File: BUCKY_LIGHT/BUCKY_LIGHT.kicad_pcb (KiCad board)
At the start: 2 copper layers, 145 x 130 mm, 150 parts, among them J1 CAN_CONN, J2 SERIAL_CONN, Q1 Q_Photo_NPN, Q10 Q_Photo_NPN, Q11 Q_Photo_NPN, Q12 Q_Photo_NPN, Q13 Q_Photo_NPN, Q14 Q_Photo_NPN, Q15 Q_Photo_NPN, Q16 Q_Photo_NPN, Q17 Q_Photo_NPN, Q18 Q_Photo_NPN, Q19 Q_Photo_NPN, Q2 Q_Photo_NPN, Q20 Q_Photo_NPN, Q21 Q_Photo_NPN, Q22 Q_Photo_NPN, Q23 Q_Photo_NPN, Q24 Q_Photo_NPN, Q25 Q_Photo_NPN, Q26 Q_Photo_NPN, Q27 Q_Photo_NPN, Q28 Q_Photo_NPN, Q3 Q_Photo_NPN, Q4 Q_Photo_NPN, Q5 Q_Photo_NPN, Q6 Q_Photo_NPN, Q7 Q_Photo_NPN, Q8 Q_Photo_NPN, Q9 Q_Photo_NPN, U1 FRONT, U2 RIGHT, U3 DOWN, U4 LEFT, U5 SN65HVD230, U6 ESP32-WROOM-32U

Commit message: Some IR changes
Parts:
- removed C1, C10, C11, C12, C13, C14, C15, C16, C17, C18, C19, C2, C20, C21, C22, C23, C24, C25, C26, C27, C28, C3, C4, C5, C6, C7, C8, C9: 0.1u, Capacitor_SMD:C_0805_2012Metric_Pad1.18x1.45mm_HandSolder
- removed R65: 120R, Resistor_SMD:R_0805_2012Metric_Pad1.20x1.40mm_HandSolder
- removed R66: 10k, Resistor_SMD:R_0805_2012Metric_Pad1.20x1.40mm_HandSolder
- moved J1 103.7 mm to (158.1, 106.5)

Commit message: Some LIGHT dev
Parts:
- added C1: 22u, Capacitor_SMD:C_1210_3225Metric_Pad1.33x2.70mm_HandSolder, F.Cu at (169.7, 104.8)
- added C2: 0.1u, Capacitor_SMD:C_1210_3225Metric_Pad1.33x2.70mm_HandSolder, F.Cu at (159.8, 113.1)
- added C3: 10u, Capacitor_SMD:C_1210_3225Metric_Pad1.33x2.70mm_HandSolder, F.Cu at (175.7, 104.8)
- added C4: 0.1u, Capacitor_SMD:C_1210_3225Metric_Pad1.33x2.70mm_HandSolder, F.Cu at (165.8, 113.1)
- added R65: 120R, Resistor_SMD:R_0805_2012Metric_Pad1.20x1.40mm_HandSolder, F.Cu at (169.0, 108.5)
- added R66: 10k, Resistor_SMD:R_0805_2012Metric_Pad1.20x1.40mm_HandSolder, F.Cu at (171.2, 111.4)
- added U7: AMS1117-3.3, Package_TO_SOT_SMD:SOT-223-3_TabPin2, F.Cu at (161.7, 106.8)
- U5, U6: moved to B.Cu
- moved J2 43.1 mm to (111.5, 118.2), turned to -90 degrees
- moved J1 14.8 mm to (143.4, 108.0)
- moved U6 14.1 mm to (143.3, 90.6), turned to 180 degrees
- moved U5 12.9 mm to (143.2, 119.8), turned to 180 degrees
- moved R54 0.81 mm to (178.5, 161.0)
- moved R38 0.76 mm to (185.5, 48.0)
- moved R8 0.76 mm to (101.0, 159.5)
- moved R14 0.72 mm to (76.5, 129.0)
- moved R5 0.70 mm to (139.8, 161.0)
- moved R55 0.70 mm to (166.2, 161.0)
- moved R56 0.70 mm to (153.3, 161.0)
- moved R6 0.70 mm to (126.3, 161.0)
- moved R7 0.70 mm to (113.3, 161.0)
- moved R15 0.67 mm to (73.0, 115.5)
- moved R37 0.64 mm to (173.5, 41.0)
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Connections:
- R13 pad 1: +3V3 -> +5V
- R14 pad 1: +3V3 -> +5V
- R15 pad 1: +3V3 -> +5V
- R16 pad 1: +3V3 -> +5V
- R21 pad 1: +3V3 -> +5V
- R22 pad 1: +3V3 -> +5V
- R23 pad 1: +3V3 -> +5V
- R24 pad 1: +3V3 -> +5V
- R29 pad 1: +3V3 -> +5V
- R30 pad 1: +3V3 -> +5V
- R31 pad 1: +3V3 -> +5V
- R32 pad 1: +3V3 -> +5V
- R37 pad 1: +3V3 -> +5V
- R38 pad 1: +3V3 -> +5V
- R39 pad 1: +3V3 -> +5V
- R40 pad 1: +3V3 -> +5V
- R45 pad 1: +3V3 -> +5V
- R46 pad 1: +3V3 -> +5V
- R47 pad 1: +3V3 -> +5V
- R48 pad 1: +3V3 -> +5V
- R5 pad 1: +3V3 -> +5V
- R53 pad 1: +3V3 -> +5V
- R54 pad 1: +3V3 -> +5V
- R55 pad 1: +3V3 -> +5V
- R56 pad 1: +3V3 -> +5V
- R6 pad 1: +3V3 -> +5V
- R7 pad 1: +3V3 -> +5V
- R8 pad 1: +3V3 -> +5V
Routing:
- net +5V: track 0.00 -> 881.1 mm, vias 0 -> 32
- net +3V3: track 0.00 -> 400.3 mm, vias 0 -> 28
- net Net-(D4-Pad2): track 0.00 -> 3.62 mm
- net Net-(D16-Pad2): track 0.00 -> 3.20 mm
- net Net-(D26-Pad2): track 0.00 -> 3.07 mm
- net Net-(D20-Pad2): track 0.00 -> 3.00 mm
- net Net-(D21-Pad2): track 0.00 -> 2.95 mm
- net Net-(D14-Pad2): track 0.00 -> 2.94 mm
- net Net-(D7-Pad2): track 0.00 -> 2.86 mm
- net Net-(D22-Pad2): track 0.00 -> 2.76 mm
- net Net-(D3-Pad2): track 0.00 -> 2.74 mm
- net Net-(D2-Pad2): track 0.00 -> 2.70 mm
- net Net-(D1-Pad2): track 0.00 -> 2.68 mm
- net Net-(D27-Pad2): track 0.00 -> 2.67 mm
- net Net-(D28-Pad2): track 0.00 -> 2.66 mm
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
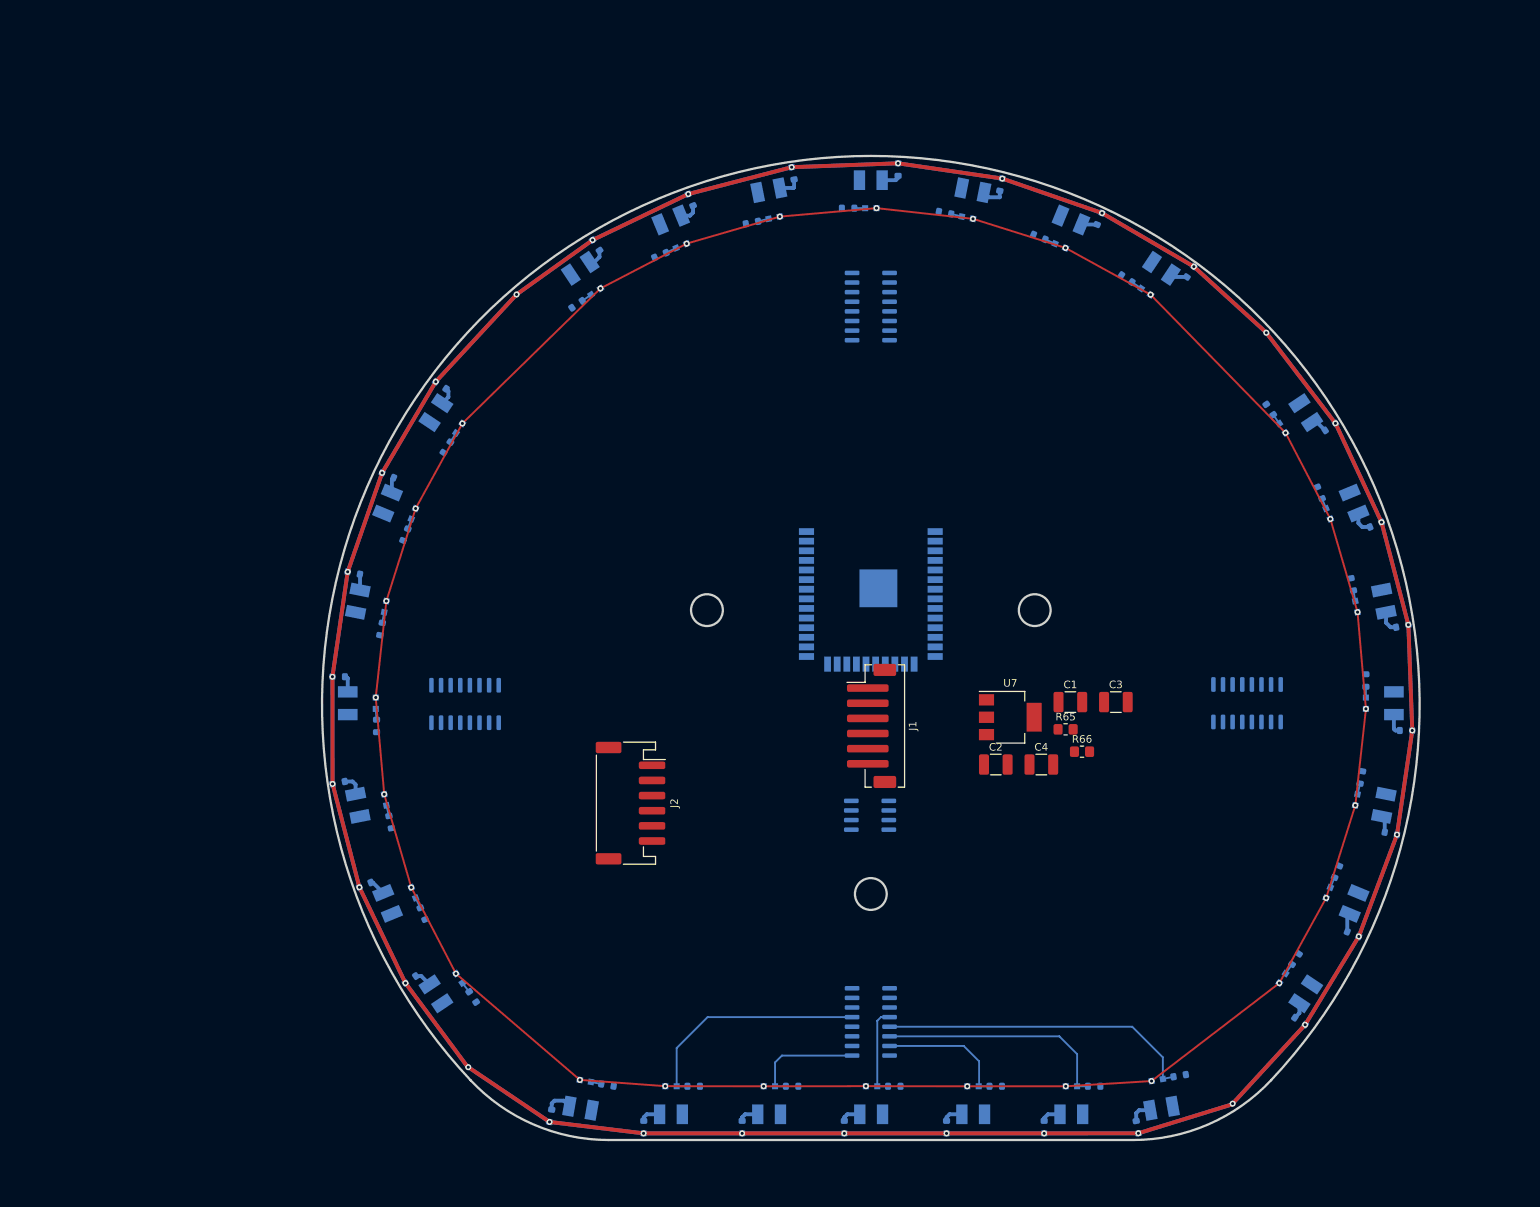
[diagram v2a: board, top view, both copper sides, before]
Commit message: Finished bulk of LIGHT, only REF left
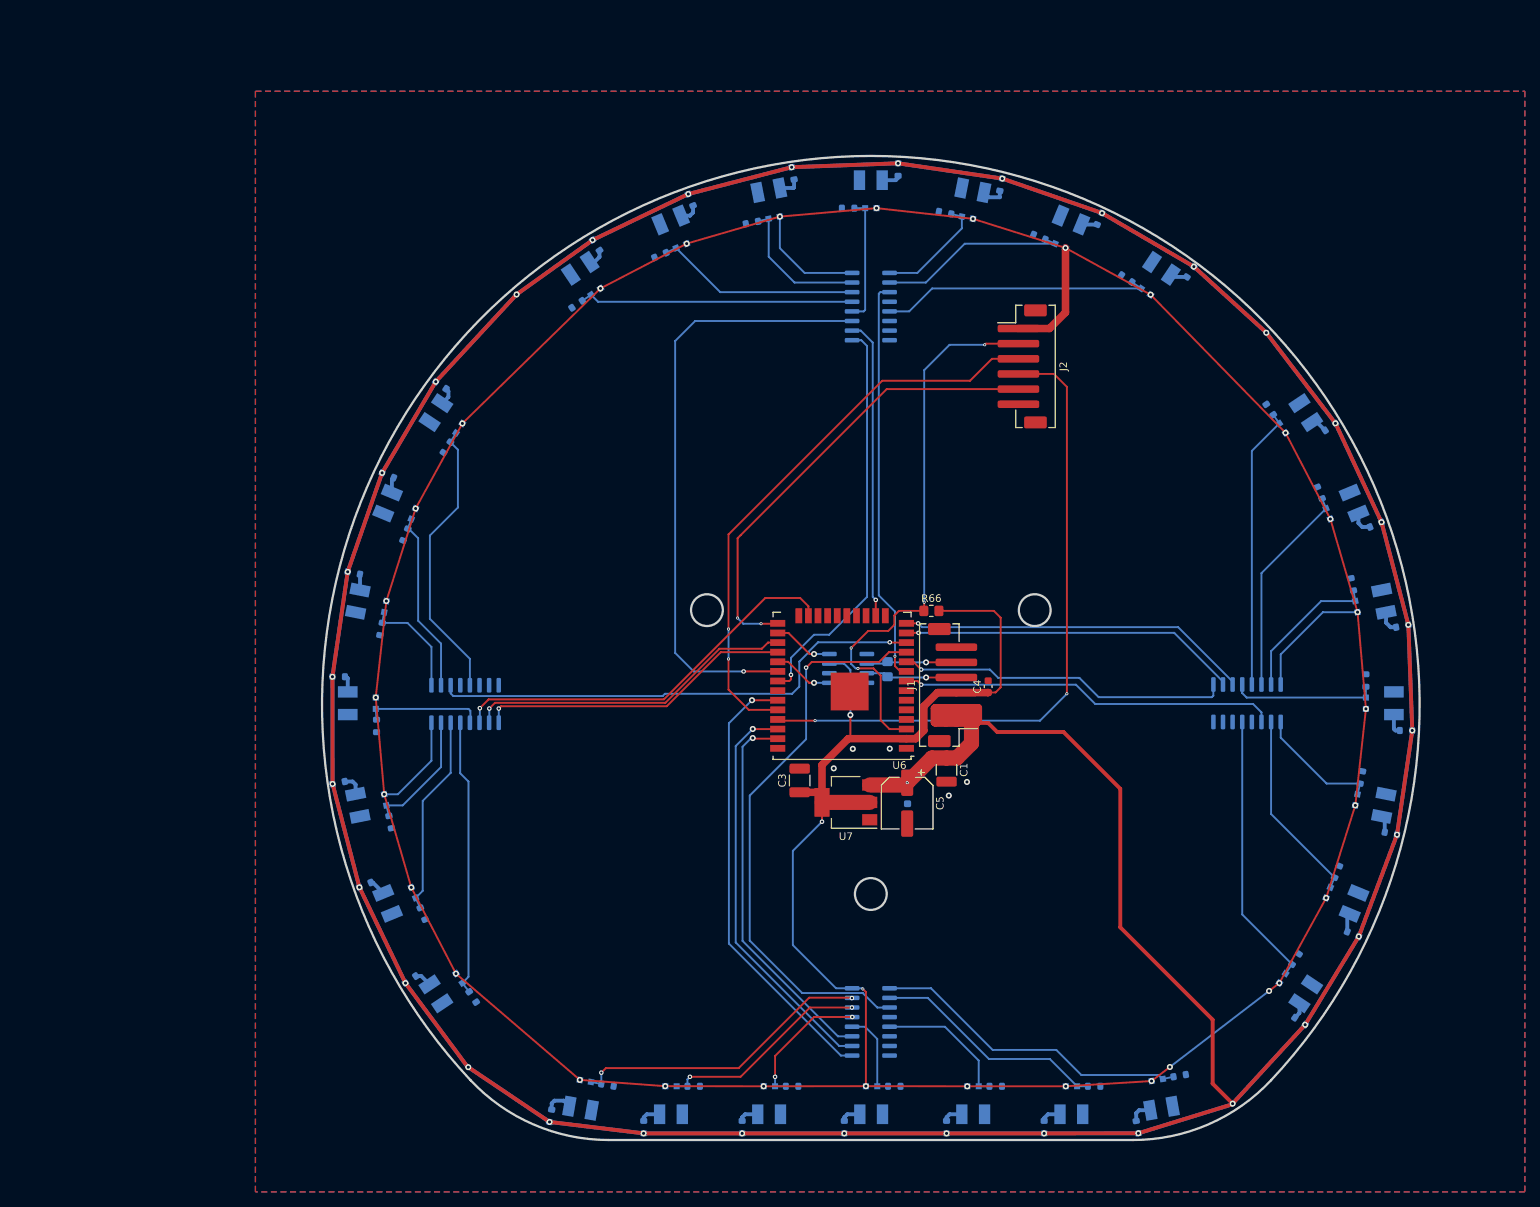
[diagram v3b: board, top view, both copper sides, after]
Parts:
- added C5: 100u, Capacitor_SMD:CP_Elec_6.3x7.7, F.Cu at (148.1, 118.2)
- C2: footprint Capacitor_SMD:C_1210_3225Metric_Pad1.33x2.70mm_HandSolder -> Capacitor_SMD:C_0603_1608Metric; moved to B.Cu
- C4: footprint Capacitor_SMD:C_1210_3225Metric_Pad1.33x2.70mm_HandSolder -> Capacitor_SMD:C_0603_1608Metric
- J2: footprint Connector_JST:JST_PH_S6B-PH-SM4-TB_1x06-1MP_P2.00mm_Horizontal -> Connector_JST:JST_PH_B6B-PH-SM4-TB_1x06-1MP_P2.00mm_Vertical
- R65: moved to B.Cu
- U6: moved to F.Cu
- moved J2 77.5 mm to (163.3, 60.5)
- moved C3 43.0 mm to (133.9, 115.2), turned to 90 degrees
- moved R66 27.2 mm to (151.3, 92.8)
- moved R65 24.8 mm to (145.5, 100.5), turned to 90 degrees
- moved U7 24.5 mm to (140.0, 118.1), turned to 180 degrees
- moved U5 19.6 mm to (140.3, 100.4), turned to 0 degrees
- moved C1 18.6 mm to (153.3, 113.8), turned to -90 degrees
- moved U6 12.7 mm to (139.5, 102.7)
- moved C4 12.5 mm to (158.8, 102.8), turned to 90 degrees
- moved C2 12.5 mm to (148.2, 117.5), turned to -90 degrees
- moved J1 12.0 mm to (154.1, 102.6), turned to 90 degrees
- turned U1 to 180 degrees
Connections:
- U1 pad 1: L2 -> L26
- U1 pad 13: L26 -> L2
- U1 pad 14: L27 -> L3
- U1 pad 15: L28 -> L4
- U1 pad 2: L4 -> L27
- U1 pad 5: L3 -> L28
- U2 pad 2: L11 -> L10
- U2 pad 5: L10 -> L11
- U3 pad 2: L18 -> L17
- U3 pad 5: L17 -> L18
- U4 pad 2: L25 -> L24
- U4 pad 5: L24 -> L25
- U6 pad 10: D_S2 -> L_S2
- U6 pad 13: F_S2 -> L_S1
- U6 pad 14: F_S0 -> L_S0
- U6 pad 16: F_S1 -> D_S1
- U6 pad 26: unconnected-(U6-Pad26) -> /CAN_RX
- U6 pad 29: unconnected-(U6-Pad29) -> /CAN_TX
- U6 pad 30: L_S0 -> D_S0
- U6 pad 31: L_S1 -> D_S2
- U6 pad 33: L_S2 -> F_S2
- U6 pad 36: D_S0 -> F_S1
- U6 pad 37: D_S1 -> F_S0
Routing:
- net +3V3: track 400.3 -> 579.7 mm, vias 28 -> 33
- net +5V: track 881.1 -> 1000.5 mm, vias 32 -> 33
- net /TX: track 0.00 -> 87.4 mm, vias 0 -> 2
- net D_S0: track 0.00 -> 80.2 mm, vias 0 -> 1
- net /RX: track 0.00 -> 76.0 mm, vias 0 -> 2
- net F_A: track 0.00 -> 75.4 mm, vias 0 -> 1
- net /EN: track 0.00 -> 74.5 mm, vias 0 -> 4
- net R_A: track 0.00 -> 66.4 mm, vias 0 -> 1
- net /IO_0: track 0.00 -> 61.4 mm, vias 0 -> 2
- net F_S2: track 0.00 -> 59.2 mm, vias 0 -> 1
- net D_S2: track 0.00 -> 53.5 mm, vias 0 -> 1
- net F_S1: track 0.00 -> 53.5 mm, vias 0 -> 1
- net D_A: track 0.00 -> 53.4 mm, vias 0 -> 1
- net R_S0: track 0.00 -> 53.1 mm, vias 0 -> 1
- net F_S0: track 0.00 -> 50.5 mm, vias 0 -> 1
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- added copper zone on B.Cu, net GND
- added copper zone on F.Cu, net GND

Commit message: Finished PCBS
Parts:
- added REF**: KiCad-Logo2_5mm_SilkScreen, Symbol:KiCad-Logo2_5mm_SilkScreen, F.Cu at (143.2, 147.8)
- added REF**: OSHW-Logo2_14.6x12mm_SilkScreen, Symbol:OSHW-Logo2_14.6x12mm_SilkScreen, F.Cu at (144.2, 53.6)
- moved C2 1.91 mm to (148.0, 115.6)
- moved C5 0.80 mm to (148.1, 117.4)
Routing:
- net GND: track 0.00 -> 1.25 mm
- net +5V: track 1000.5 -> 999.3 mm
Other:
- board text added: "BUCKY AMBIENT LIGHT BOARD DESIGNED BY PIXELJOCH 01-2023 V-2.0"
- board text added: "TEAM BUCKY"
- board text added: "i see the light!"

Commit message: chore: start on schematics
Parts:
- removed C1: 22u, Capacitor_SMD:C_1210_3225Metric_Pad1.33x2.70mm_HandSolder
- removed C2, C4: 0.1u, Capacitor_SMD:C_0603_1608Metric
- removed C3: 10u, Capacitor_SMD:C_1210_3225Metric_Pad1.33x2.70mm_HandSolder
- removed C5: 100u, Capacitor_SMD:CP_Elec_6.3x7.7
- removed R65: 120R, Resistor_SMD:R_0805_2012Metric_Pad1.20x1.40mm_HandSolder
- removed R66: 10k, Resistor_SMD:R_0805_2012Metric_Pad1.20x1.40mm_HandSolder
- removed REF**: KiCad-Logo2_5mm_SilkScreen, Symbol:KiCad-Logo2_5mm_SilkScreen
- removed REF**: OSHW-Logo2_14.6x12mm_SilkScreen, Symbol:OSHW-Logo2_14.6x12mm_SilkScreen
- removed U5: SN65HVD230, Package_SO:SOIC-8_3.9x4.9mm_P1.27mm
- removed U6: ESP32-WROOM-32U, RF_Module:ESP32-WROOM-32U
- removed U7: AMS1117-3.3, Package_TO_SOT_SMD:SOT-223-3_TabPin2
- J1: value CAN_CONN -> Conn_01x16; footprint Connector_JST:JST_PH_B6B-PH-SM4-TB_1x06-1MP_P2.00mm_Vertical -> BUCKY_LIGHT:BUCKY_LIGHT_POWER
- J2: value SERIAL_CONN -> Conn_01x02; footprint Connector_JST:JST_PH_B6B-PH-SM4-TB_1x06-1MP_P2.00mm_Vertical -> BUCKY_LIGHT:BUCKY_POWER_CONN
- moved J2 50.7 mm to (144.3, 107.5), turned to 180 degrees
- moved J1 12.6 mm to (143.3, 96.0), turned to 0 degrees
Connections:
- J1 pad 1: +5V -> R_A
- J1 pad 2: +5V -> R_S0
- J1 pad 3: +3V3 -> R_S1
- J1 pad 4: /CAN_H -> R_S2
- J1 pad 5: /CAN_L -> F_S2
- J1 pad 6: GND -> F_S1
- J2 pad 1: +3V3 -> +5V
- J2 pad 2: /EN -> GND
- Q1 pad 1: +3V3 -> +5V
- Q10 pad 1: +3V3 -> +5V
- Q11 pad 1: +3V3 -> +5V
- Q12 pad 1: +3V3 -> +5V
- Q13 pad 1: +3V3 -> +5V
- Q14 pad 1: +3V3 -> +5V
- Q15 pad 1: +3V3 -> +5V
- Q16 pad 1: +3V3 -> +5V
- Q17 pad 1: +3V3 -> +5V
- Q18 pad 1: +3V3 -> +5V
- Q19 pad 1: +3V3 -> +5V
- Q2 pad 1: +3V3 -> +5V
- Q20 pad 1: +3V3 -> +5V
- Q21 pad 1: +3V3 -> +5V
- Q22 pad 1: +3V3 -> +5V
- Q23 pad 1: +3V3 -> +5V
- Q24 pad 1: +3V3 -> +5V
- Q25 pad 1: +3V3 -> +5V
- Q26 pad 1: +3V3 -> +5V
- Q27 pad 1: +3V3 -> +5V
- Q28 pad 1: +3V3 -> +5V
- Q3 pad 1: +3V3 -> +5V
- Q4 pad 1: +3V3 -> +5V
- Q5 pad 1: +3V3 -> +5V
- Q6 pad 1: +3V3 -> +5V
- Q7 pad 1: +3V3 -> +5V
- Q8 pad 1: +3V3 -> +5V
- Q9 pad 1: +3V3 -> +5V
- U1 pad 16: +3V3 -> +5V
- U2 pad 16: +3V3 -> +5V
- U3 pad 16: +3V3 -> +5V
- U4 pad 16: +3V3 -> +5V
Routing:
- net +3V3: track 579.7 -> 0.00 mm, vias 33 -> 0
- net +5V: track 999.3 -> 1419.9 mm, vias 33 -> 60
- net /TX: track 87.4 -> 0.00 mm, vias 2 -> 0
- net /RX: track 76.0 -> 0.00 mm, vias 2 -> 0
- net /EN: track 74.5 -> 0.00 mm, vias 4 -> 0
- net /IO_0: track 61.4 -> 0.00 mm, vias 2 -> 0
- net D_S0: track 80.2 -> 44.8 mm
- net F_A: track 75.4 -> 49.6 mm
- net R_A: track 66.4 -> 43.5 mm
- net D_S2: track 53.5 -> 39.9 mm
- net /CAN_H: track 12.1 -> 0.00 mm, vias 1 -> 0
- net /CAN_L: track 12.0 -> 0.00 mm, vias 1 -> 0
- net L_S0: track 46.7 -> 37.3 mm
- net /CAN_RX: track 7.98 -> 0.00 mm, vias 1 -> 0
- net /CAN_TX: track 7.98 -> 0.00 mm, vias 1 -> 0
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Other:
- board text added: "BUCKY AMBIENT LIGHT BOARD DESIGNED BY KOEN_1711 01-2023 V-1.0"
- board text added: "if you didn't notice, i am upside down"
- board text removed: "BUCKY AMBIENT LIGHT BOARD DESIGNED BY PIXELJOCH 01-2023 V-2.0"

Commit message: chore: finish main board
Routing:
- net +5V: track 1419.9 -> 1404.3 mm
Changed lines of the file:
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@@
 			)
 		)
+		(property "Field5" ""
+			(at 0 0 0)
+			(unlocked yes)
+			(layer "F.Fab")
+			(hide yes)
+			(effects
+				(font
+					(size 1 1)
+					(thickness 0.15)
+				)
+			)
+		)
 		(property ki_fp_filters "Connector*:*_1x??_*")
-		(sheetname "Root")
-		(sheetfile "BUCKY_LIGHT.kicad_sch")
+		(sheetname "CONNECTORS")
+		(sheetfile "CONN.kicad_sch")
 		(attr smd)
 		(fp_circle
@@
 		)
 		(property ki_fp_filters "Connector*:*_1x??_*")
-		(sheetname "Root")
-		(sheetfile "BUCKY_LIGHT.kicad_sch")
+		(sheetname "CONNECTORS")
+		(sheetfile "CONN.kicad_sch")
 		(attr through_hole)
 		(fp_circle
@@
 	)
 	(segment
-		(start 169.016731 53.383269)
-		(end 169.016731 44.850038)
-		(width 1)
-		(layer "F.Cu")
-		(net 82)
-	)
-	(segment
 		(start 96.50357 50.996583)
 		(end 106.545225 43.810621)
@@
 	)
 	(segment
-		(start 162.8 55.5)
-		(end 166.9 55.5)
-		(width 1)
-		(layer "F.Cu")
-		(net 82)
-	)
-	(segment
 		(start 207.765771 135.812297)
 		(end 200.689532 147.454928)
@@
 		(layer "F.Cu")
 		(net 82)
-	)
-	(segment
-		(start 166.9 55.5)
-		(end 169.016731 53.383269)
-		(width 1)
-		(layer "F.Cu")
-		(net 82)
